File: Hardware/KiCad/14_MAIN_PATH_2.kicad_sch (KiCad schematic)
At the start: 0 parts

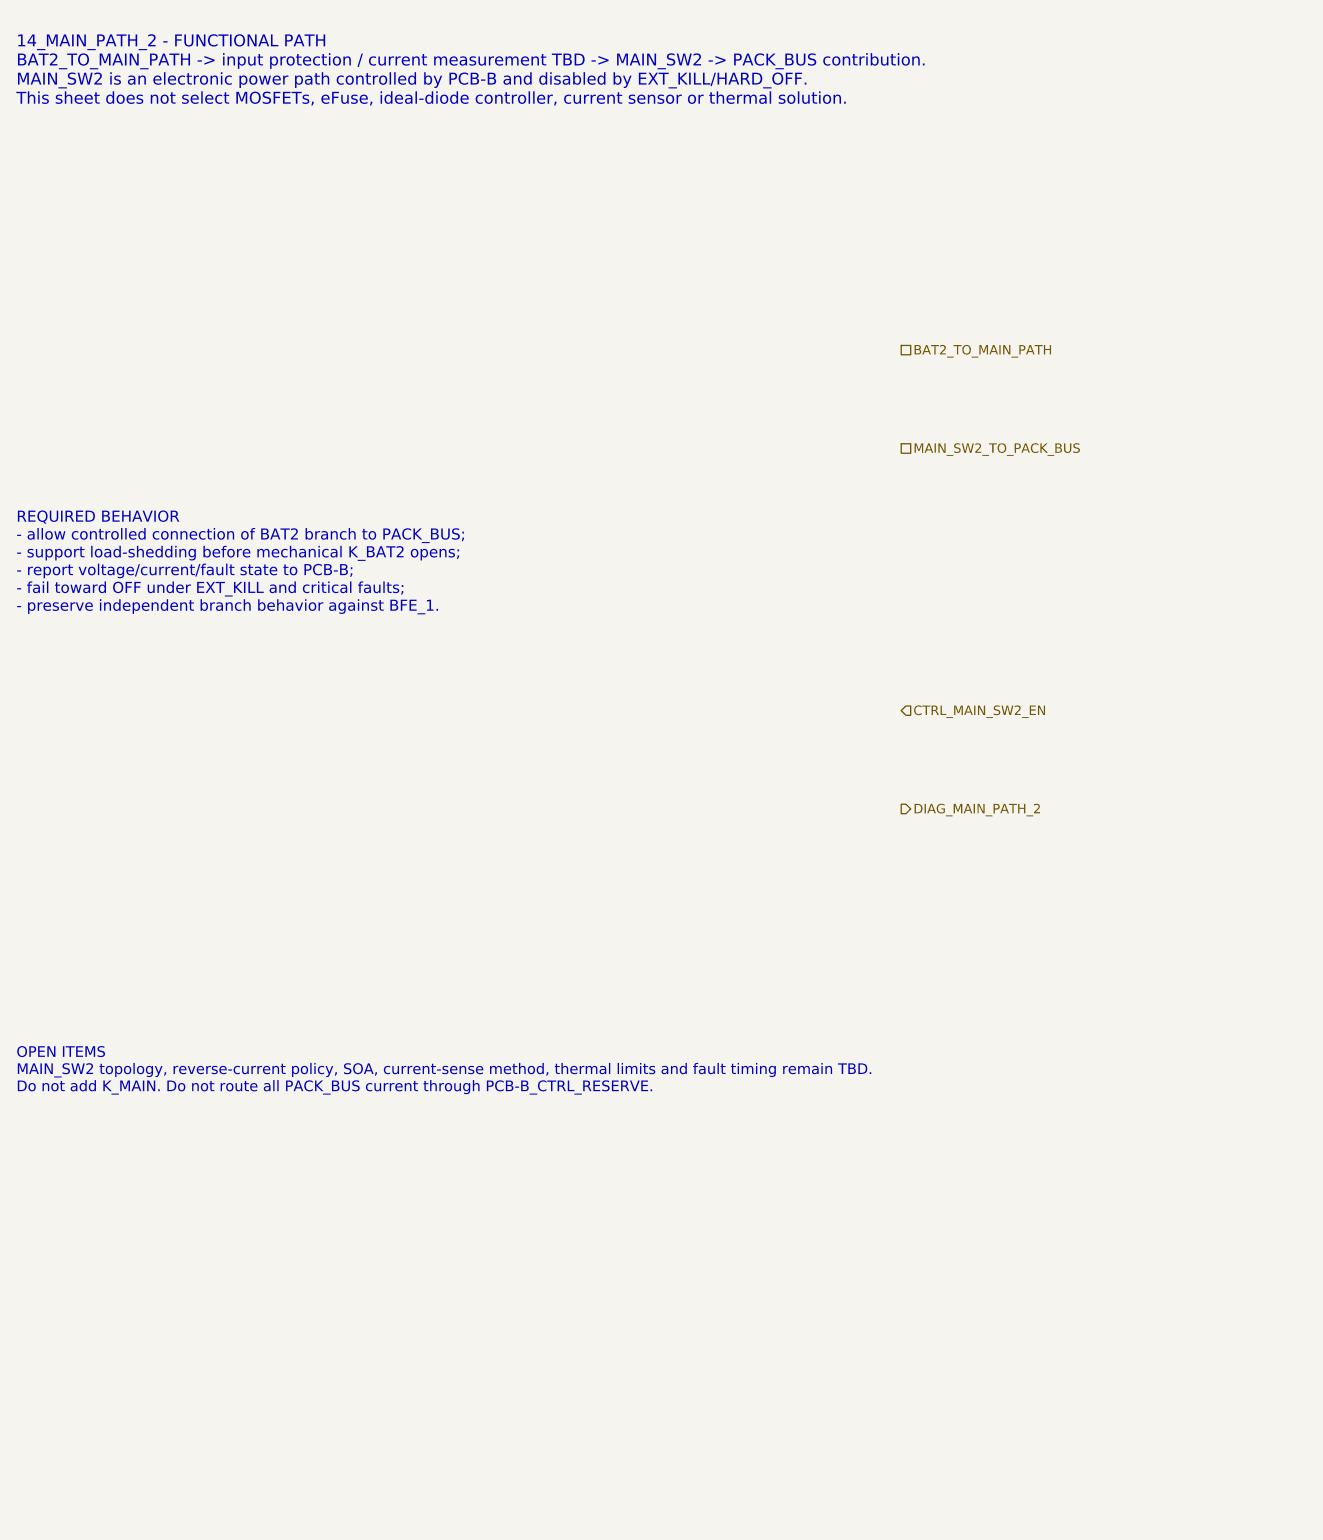
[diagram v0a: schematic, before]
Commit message: hardware: refine MAIN_PATH_2 level B
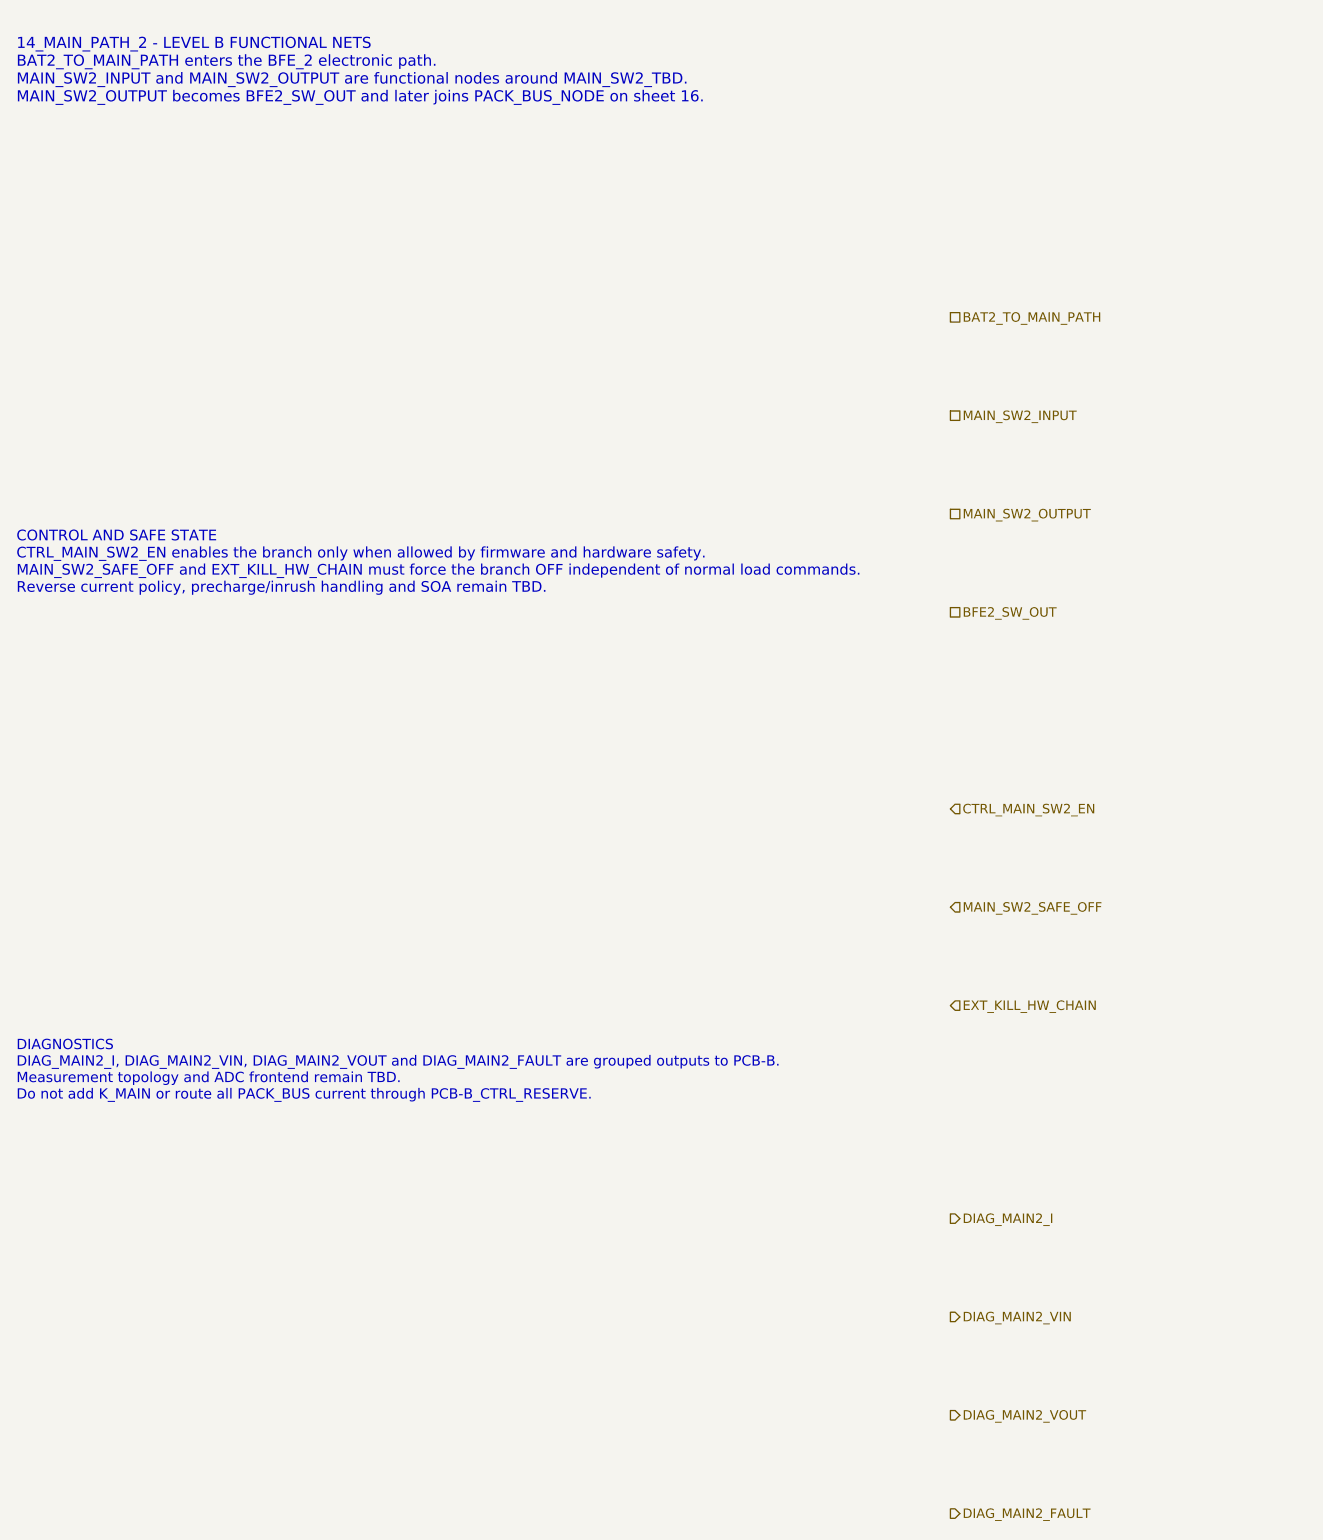
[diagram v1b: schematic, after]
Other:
- note added: "14_MAIN_PATH_2 - LEVEL B FUNCTIONAL NETS BAT2_TO_MAIN_PATH enters the BFE_2 electronic path. MAIN_SW2_INPUT and MAIN_SW2_OUTPUT are functional nodes around MAIN_SW2_TBD. MAIN_SW2_OUTPUT becomes BFE2_SW_OUT and later joins PACK_BUS_NODE on sheet 16."
- note added: "CONTROL AND SAFE STATE CTRL_MAIN_SW2_EN enables the branch only when allowed by firmware and hardware safety. MAIN_SW2_SAFE_OFF and EXT_KILL_HW_CHAIN must force the branch OFF independent of normal load commands. Reverse current policy, precharge/inrush handling and SOA remain TBD."
- note added: "DIAGNOSTICS DIAG_MAIN2_I, DIAG_MAIN2_VIN, DIAG_MAIN2_VOUT and DIAG_MAIN2_FAULT are grouped outputs to PCB-B. Measurement topology and ADC frontend remain TBD. Do not add K_MAIN or route all PACK_BUS current through PCB-B_CTRL_RESERVE."
- note removed: "14_MAIN_PATH_2 - FUNCTIONAL PATH BAT2_TO_MAIN_PATH -> input protection / current measurement TBD -> MAIN_SW2 -> PACK_BUS contribution. MAIN_SW2 is an electronic power path controlled by PCB-B and disabled by EXT_KILL/HARD_OFF. This sheet does not select MOSFETs, eFuse, ideal-diode controller, current sensor or thermal solution."
- note removed: "OPEN ITEMS MAIN_SW2 topology, reverse-current policy, SOA, current-sense method, thermal limits and fault timing remain TBD. Do not add K_MAIN. Do not route all PACK_BUS current through PCB-B_CTRL_RESERVE."
- note removed: "REQUIRED BEHAVIOR - allow controlled connection of BAT2 branch to PACK_BUS; - support load-shedding before mechanical K_BAT2 opens; - report voltage/current/fault state to PCB-B; - fail toward OFF under EXT_KILL and critical faults; - preserve independent branch behavior against BFE_1."
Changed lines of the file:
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@@
 	(generator "eeschema")
 	(generator_version "10.0")
-	(uuid "bfe-dh-00000014-0000-4000-8000-000000000014")
+	(uuid "bfe-lb-00000014-0000-4000-8000-000000000014")
 	(paper "A3")
 	(title_block
 		(title "14_MAIN_PATH_2 - BFE_2 main electronic path")
 		(date "2026-07-15")
-		(rev "A1")
+		(rev "B1")
 		(company "Gonoboben/plataVM")
-		(comment 1 "Architecture Level A: MAIN_SW2 functional boundary")
+		(comment 1 "Architecture Level B: MAIN_SW2 control, diagnostics and safe-state nets")
 		(comment 2 "Symmetric to 13_MAIN_PATH_1; no MAIN_SW2 topology selected")
 	)
-	(text "14_MAIN_PATH_2 - FUNCTIONAL PATH\nBAT2_TO_MAIN_PATH -> input protection / current measurement TBD -> MAIN_SW2 -> PACK_BUS contribution.\nMAIN_SW2 is an electronic power path controlled by PCB-B and disabled by EXT_KILL/HARD_OFF.\nThis sheet does not select MOSFETs, eFuse, ideal-diode controller, current sensor or thermal solution."
+	(text "14_MAIN_PATH_2 - LEVEL B FUNCTIONAL NETS\nBAT2_TO_MAIN_PATH enters the BFE_2 electronic path.\nMAIN_SW2_INPUT and MAIN_SW2_OUTPUT are functional nodes around MAIN_SW2_TBD.\nMAIN_SW2_OUTPUT becomes BFE2_SW_OUT and later joins PACK_BUS_NODE on sheet 16."
 		(exclude_from_sim no)
 		(at 12 18 0)
-		(effects (font (size 1.45 1.45)) (justify left))
-		(uuid "bfe-dh-00000014-0000-4000-8000-000000000101")
+		(effects (font (size 1.35 1.35)) (justify left))
+		(uuid "bfe-lb-00000014-0000-4000-8000-000000000101")
 	)
-	(text "REQUIRED BEHAVIOR\n- allow controlled connection of BAT2 branch to PACK_BUS;\n- support load-shedding before mechanical K_BAT2 opens;\n- report voltage/current/fault state to PCB-B;\n- fail toward OFF under EXT_KILL and critical faults;\n- preserve independent branch behavior against BFE_1."
+	(text "CONTROL AND SAFE STATE\nCTRL_MAIN_SW2_EN enables the branch only when allowed by firmware and hardware safety.\nMAIN_SW2_SAFE_OFF and EXT_KILL_HW_CHAIN must force the branch OFF independent of normal load commands.\nReverse current policy, precharge/inrush handling and SOA remain TBD."
 		(exclude_from_sim no)
 		(at 12 78 0)
-		(effects (font (size 1.35 1.35)) (justify left))
-		(uuid "bfe-dh-00000014-0000-4000-8000-000000000102")
+		(effects (font (size 1.3 1.3)) (justify left))
+		(uuid "bfe-lb-00000014-0000-4000-8000-000000000102")
 	)
-	(text "OPEN ITEMS\nMAIN_SW2 topology, reverse-current policy, SOA, current-sense method, thermal limits and fault timing remain TBD.\nDo not add K_MAIN. Do not route all PACK_BUS current through PCB-B_CTRL_RESERVE."
+	(text "DIAGNOSTICS\nDIAG_MAIN2_I, DIAG_MAIN2_VIN, DIAG_MAIN2_VOUT and DIAG_MAIN2_FAULT are grouped outputs to PCB-B.\nMeasurement topology and ADC frontend remain TBD.\nDo not add K_MAIN or route all PACK_BUS current through PCB-B_CTRL_RESERVE."
 		(exclude_from_sim no)
 		(at 12 140 0)
-		(effects (font (size 1.3 1.3)) (justify left))
-		(uuid "bfe-dh-00000014-0000-4000-8000-000000000103")
+		(effects (font (size 1.25 1.25)) (justify left))
+		(uuid "bfe-lb-00000014-0000-4000-8000-000000000103")
 	)
-	(hierarchical_label "BAT2_TO_MAIN_PATH" (shape passive) (exclude_from_sim no) (at 120 52 0) (effects (font (size 1.15 1.15)) (justify left)) (uuid "bfe-dh-00000014-0000-4000-8000-000000000201"))
-	(hierarchical_label "MAIN_SW2_TO_PACK_BUS" (shape passive) (exclude_from_sim no) (at 120 64 0) (effects (font (size 1.15 1.15)) (justify left)) (uuid "bfe-dh-00000014-0000-4000-8000-000000000202"))
-	(hierarchical_label "CTRL_MAIN_SW2_EN" (shape input) (exclude_from_sim no) (at 120 96 0) (effects (font (size 1.15 1.15)) (justify left)) (uuid "bfe-dh-00000014-0000-4000-8000-000000000203"))
-	(hierarchical_label "DIAG_MAIN_PATH_2" (shape output) (exclude_from_sim no) (at 120 108 0) (effects (font (size 1.15 1.15)) (justify left)) (uuid "bfe-dh-00000014-0000-4000-8000-000000000204"))
+	(hierarchical_label "BAT2_TO_MAIN_PATH" (shape passive) (exclude_from_sim no) (at 126 48 0) (effects (font (size 1.15 1.15)) (justify left)) (uuid "bfe-lb-00000014-0000-4000-8000-000000000201"))
+	(hierarchical_label "MAIN_SW2_INPUT" (shape passive) (exclude_from_sim no) (at 126 60 0) (effects (font (size 1.15 1.15)) (justify left)) (uuid "bfe-lb-00000014-0000-4000-8000-000000000202"))
+	(hierarchical_label "MAIN_SW2_OUTPUT" (shape passive) (exclude_from_sim no) (at 126 72 0) (effects (font (size 1.15 1.15)) (justify left)) (uuid "bfe-lb-00000014-0000-4000-8000-000000000203"))
+	(hierarchical_label "BFE2_SW_OUT" (shape passive) (exclude_from_sim no) (at 126 84 0) (effects (font (size 1.15 1.15)) (justify left)) (uuid "bfe-lb-00000014-0000-4000-8000-000000000204"))
+	(hierarchical_label "CTRL_MAIN_SW2_EN" (shape input) (exclude_from_sim no) (at 126 108 0) (effects (font (size 1.15 1.15)) (justify left)) (uuid "bfe-lb-00000014-0000-4000-8000-000000000205"))
+	(hierarchical_label "MAIN_SW2_SAFE_OFF" (shape input) (exclude_from_sim no) (at 126 120 0) (effects (font (size 1.15 1.15)) (justify left)) (uuid "bfe-lb-00000014-0000-4000-8000-000000000206"))
+	(hierarchical_label "EXT_KILL_HW_CHAIN" (shape input) (exclude_from_sim no) (at 126 132 0) (effects (font (size 1.15 1.15)) (justify left)) (uuid "bfe-lb-00000014-0000-4000-8000-000000000207"))
+	(hierarchical_label "DIAG_MAIN2_I" (shape output) (exclude_from_sim no) (at 126 158 0) (effects (font (size 1.15 1.15)) (justify left)) (uuid "bfe-lb-00000014-0000-4000-8000-000000000208"))
+	(hierarchical_label "DIAG_MAIN2_VIN" (shape output) (exclude_from_sim no) (at 126 170 0) (effects (font (size 1.15 1.15)) (justify left)) (uuid "bfe-lb-00000014-0000-4000-8000-000000000209"))
+	(hierarchical_label "DIAG_MAIN2_VOUT" (shape output) (exclude_from_sim no) (at 126 182 0) (effects (font (size 1.15 1.15)) (justify left)) (uuid "bfe-lb-00000014-0000-4000-8000-000000000210"))
+	(hierarchical_label "DIAG_MAIN2_FAULT" (shape output) (exclude_from_sim no) (at 126 194 0) (effects (font (size 1.15 1.15)) (justify left)) (uuid "bfe-lb-00000014-0000-4000-8000-000000000211"))
 )
